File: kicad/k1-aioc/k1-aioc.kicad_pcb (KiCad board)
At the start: 2 copper layers, 50.8 x 71.1 mm, 56 parts, among them J1 Conn_01x07_Male, J2 12401832E402A, J3 SIP 200, J4 SIP 200, Q1 BC847BS, U1 MIC5330-SSYML, U2 STM32F373CBTx(OLD), Y1 8MHz/20pF

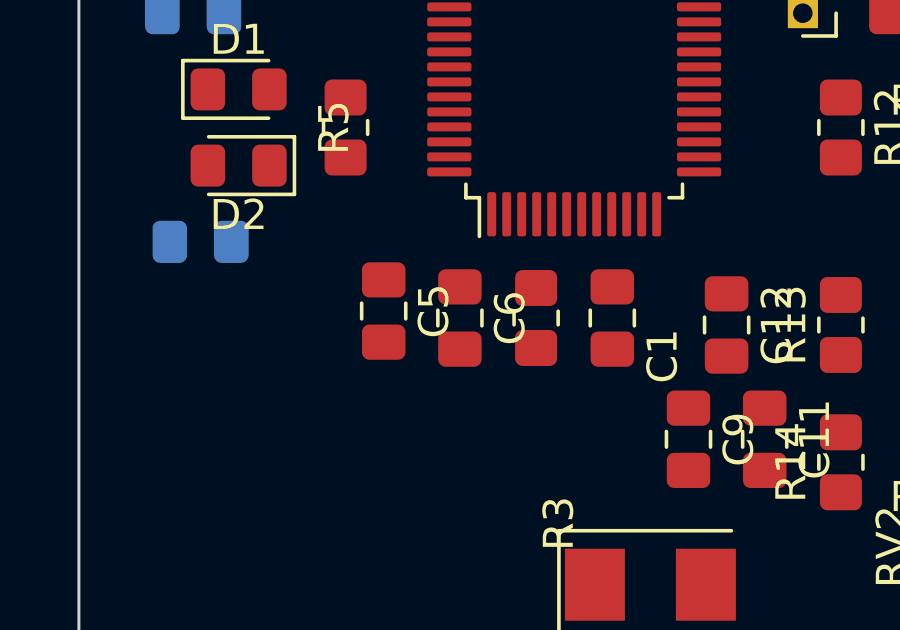
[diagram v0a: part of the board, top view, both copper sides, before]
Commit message: updating files and adding usb datasheet
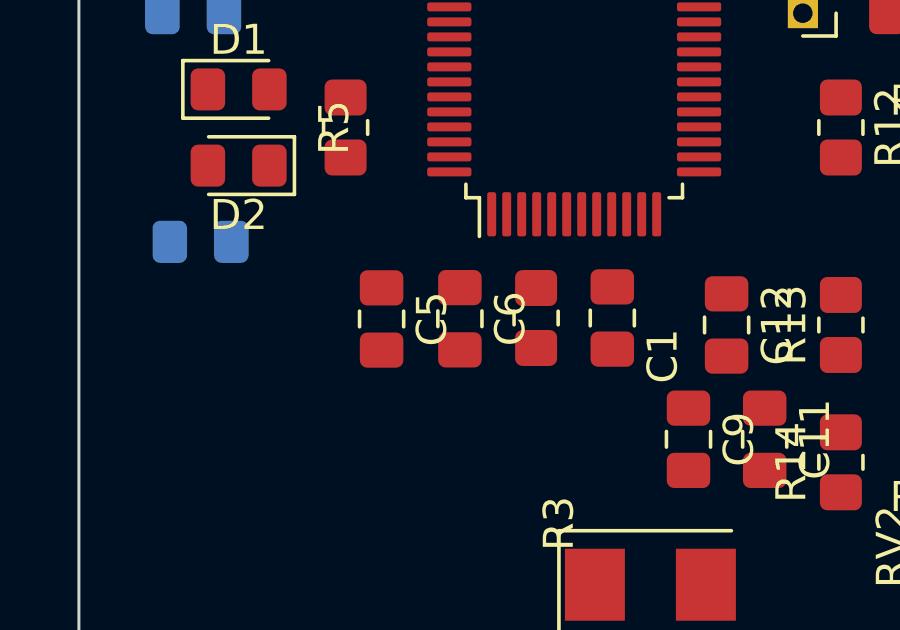
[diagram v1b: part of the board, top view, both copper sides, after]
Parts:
- moved C5 0.27 mm to (123.8, 97.6)
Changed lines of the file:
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@@
   )
   (footprint "Capacitor_SMD:C_0805_2012Metric_Pad1.18x1.45mm_HandSolder" (layer "F.Cu")
-    (at 126.36 97.53 -90)
+    (at 126.36 97.555 -90)
     (descr "Capacitor SMD 0805 (2012 Metric), square (rectangular) end terminal, IPC_7351 nominal with elongated pad for handsoldering. (Body size source: IPC-SM-782 page 76, https://www.pcb-3d.com/wordpress/wp-content/uploads/ipc-sm-782a_amendment_1_and_2.pdf, https://docs.google.com/spreadsheets/d/1BsfQQcO9C6DZCsRaXUlFlo91Tg2WpOkGARC1WS5S8t0/edit?usp=sharing), generated with kicad-footprint-generator")
     (tags "capacitor handsolder")
@@
   )
   (footprint "Capacitor_SMD:C_0805_2012Metric_Pad1.18x1.45mm_HandSolder" (layer "F.Cu")
-    (at 123.82 97.2975 -90)
+    (at 123.75 97.5625 -90)
     (descr "Capacitor SMD 0805 (2012 Metric), square (rectangular) end terminal, IPC_7351 nominal with elongated pad for handsoldering. (Body size source: IPC-SM-782 page 76, https://www.pcb-3d.com/wordpress/wp-content/uploads/ipc-sm-782a_amendment_1_and_2.pdf, https://docs.google.com/spreadsheets/d/1BsfQQcO9C6DZCsRaXUlFlo91Tg2WpOkGARC1WS5S8t0/edit?usp=sharing), generated with kicad-footprint-generator")
     (tags "capacitor handsolder")
